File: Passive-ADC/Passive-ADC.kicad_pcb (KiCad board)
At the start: 2 copper layers, 72.6 x 24.1 mm, 11 parts, among them J1 FPGA Terminal, J2 ADC Terminal

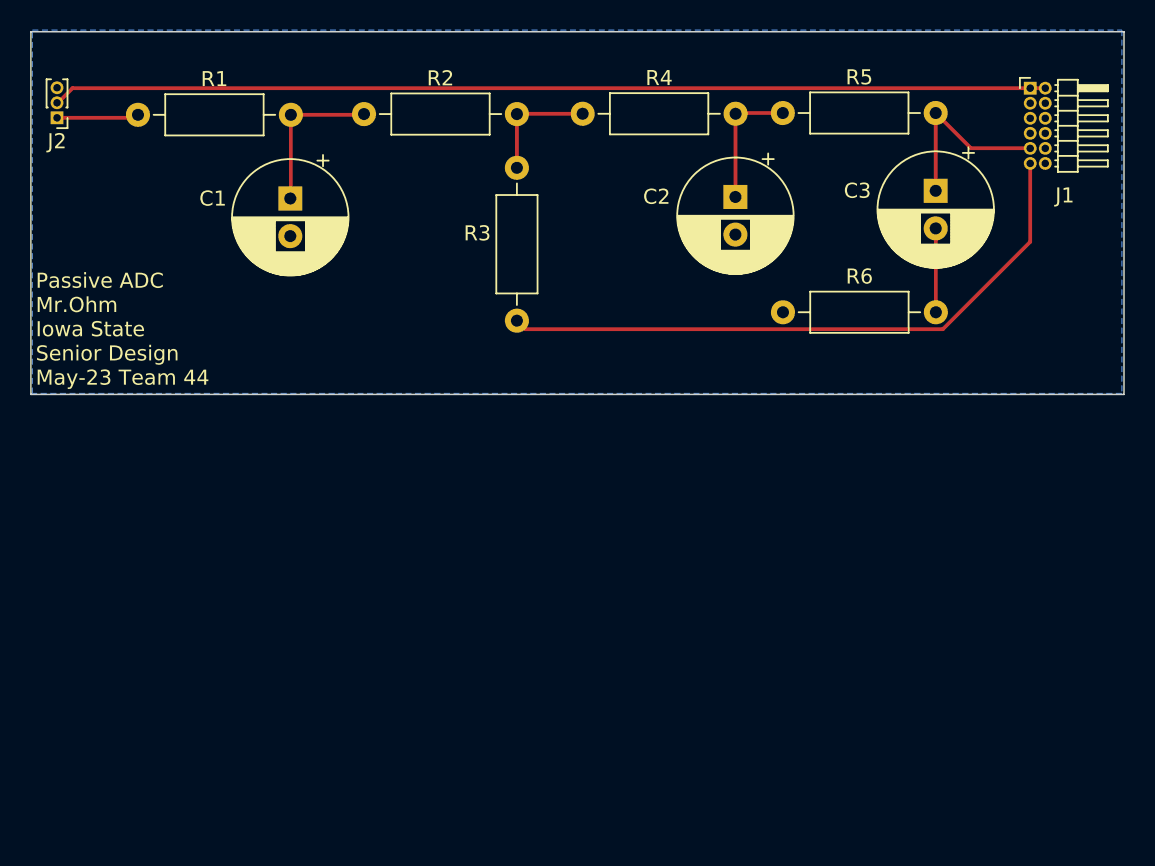
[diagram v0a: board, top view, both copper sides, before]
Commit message: Replaced passive adc with active adc
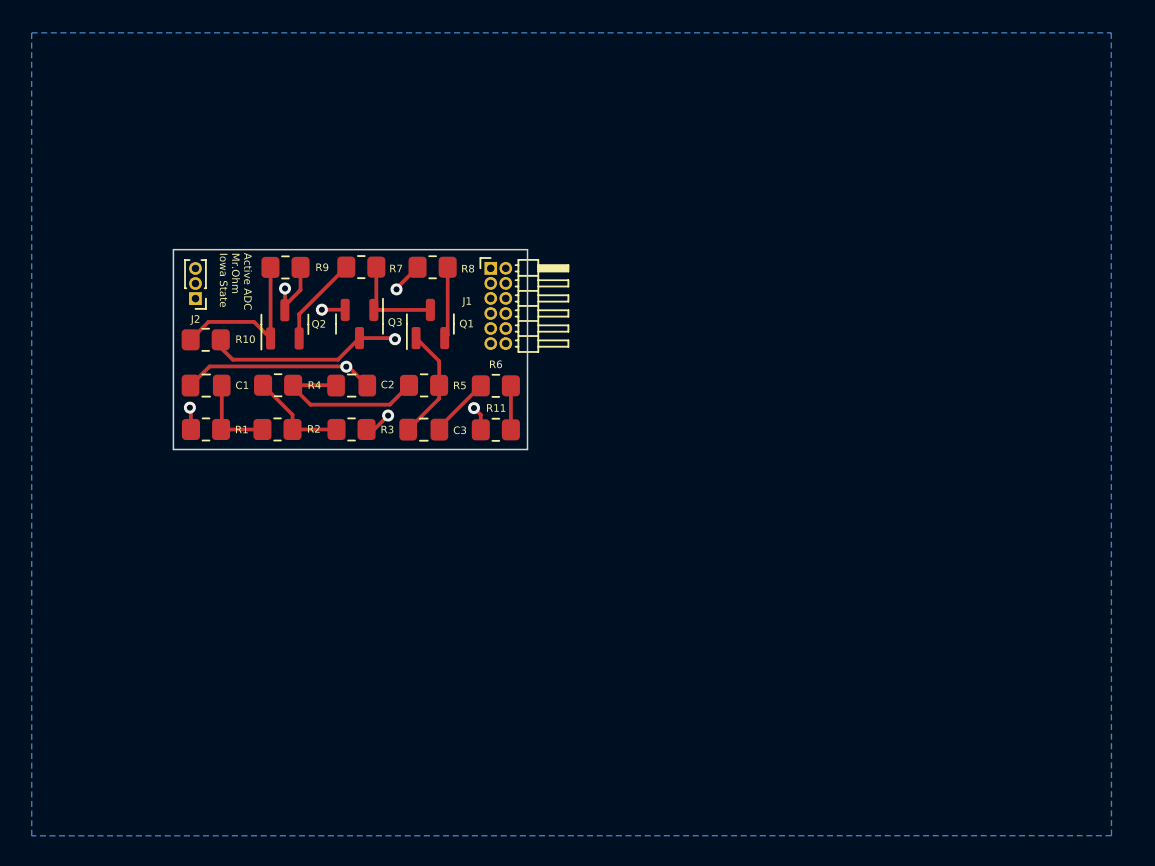
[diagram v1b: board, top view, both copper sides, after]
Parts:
- added Q1: BC847, Package_TO_SOT_SMD:SOT-23, F.Cu at (131.4, 85.2)
- added Q2: BC847, Package_TO_SOT_SMD:SOT-23, F.Cu at (121.7, 85.3)
- added Q3: BC847, Package_TO_SOT_SMD:SOT-23, F.Cu at (126.7, 85.2)
- added R10: 2.5k, Resistor_SMD:R_0805_2012Metric_Pad1.20x1.40mm_HandSolder, F.Cu at (116.5, 86.3)
- added R11: 680, Resistor_SMD:R_0805_2012Metric_Pad1.20x1.40mm_HandSolder, F.Cu at (135.7, 92.3)
- added R7: 2.1k, Resistor_SMD:R_0805_2012Metric_Pad1.20x1.40mm_HandSolder, F.Cu at (126.8, 81.5)
- added R8: 330, Resistor_SMD:R_0805_2012Metric_Pad1.20x1.40mm_HandSolder, F.Cu at (131.5, 81.5)
- added R9: 1.5k, Resistor_SMD:R_0805_2012Metric_Pad1.20x1.40mm_HandSolder, F.Cu at (121.8, 81.5)
- C1, C2, C3: footprint Capacitor_THT:CP_Radial_D7.5mm_P2.50mm -> Capacitor_SMD:C_0805_2012Metric_Pad1.18x1.45mm_HandSolder
- R1: footprint Resistor_THT:R_Axial_DIN0207_L6.3mm_D2.5mm_P10.16mm_Horizontal -> Resistor_SMD:R_0805_2012Metric_Pad1.20x1.40mm_HandSolder
- R2: value 36k -> 18k; footprint Resistor_THT:R_Axial_DIN0207_L6.3mm_D2.5mm_P10.16mm_Horizontal -> Resistor_SMD:R_0805_2012Metric_Pad1.20x1.40mm_HandSolder
- R3, R4: value 18k -> 15k; footprint Resistor_THT:R_Axial_DIN0207_L6.3mm_D2.5mm_P10.16mm_Horizontal -> Resistor_SMD:R_0805_2012Metric_Pad1.20x1.40mm_HandSolder
- R5: value 56k -> 8k; footprint Resistor_THT:R_Axial_DIN0207_L6.3mm_D2.5mm_P10.16mm_Horizontal -> Resistor_SMD:R_0805_2012Metric_Pad1.20x1.40mm_HandSolder
- R6: value 110 -> 470; footprint Resistor_THT:R_Axial_DIN0207_L6.3mm_D2.5mm_P10.16mm_Horizontal -> Resistor_SMD:R_0805_2012Metric_Pad1.20x1.40mm_HandSolder
- moved J1 37.8 mm to (135.4, 81.5)
- moved C3 37.5 mm to (130.9, 92.3), turned to 0 degrees
- moved R5 29.9 mm to (131.0, 89.3)
- moved C2 28.4 mm to (126.2, 89.3), turned to 0 degrees
- moved R4 27.1 mm to (121.3, 89.3)
- moved R2 21.7 mm to (121.2, 92.3)
- moved R1 21.4 mm to (116.5, 92.3)
- moved R6 19.7 mm to (135.7, 89.4), turned to 180 degrees
- moved J2 15.1 mm to (115.8, 83.6)
- moved C1 13.6 mm to (116.5, 89.3), turned to 180 degrees
- moved R3 13.2 mm to (126.2, 92.3), turned to 180 degrees
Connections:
- C3 pad 1: /FPGA-OUT -> /SIGMA-CHERRY
- R5 pad 2: /FPGA-OUT -> /SIGMA-CHERRY
- R6 pad 1: GND -> Net-(R6-Pad1)
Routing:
- net /3.3V: track 66.1 -> 4.72 mm, vias 0 -> 1
- net /FPGA-IN: track 42.0 -> 10.6 mm, vias 0 -> 1
- net GND: track 0.00 -> 18.0 mm, vias 0 -> 4
- net Net-(Q2-Pad1): track 0.00 -> 11.0 mm
- net /SIGMA-CHERRY: track 0.00 -> 7.57 mm
- net /FPGA-OUT: track 12.7 -> 19.7 mm, vias 0 -> 1
- net Net-(Q1-Pad3): track 0.00 -> 6.70 mm
- net Net-(Q2-Pad2): track 0.00 -> 6.04 mm
- net Net-(Q1-Pad2): track 0.00 -> 4.79 mm
- net Net-(C1-Pad1): track 10.5 -> 5.69 mm
- net /Sensor-IN: track 5.46 -> 8.88 mm, vias 0 -> 1
- net Net-(C2-Pad1): track 8.69 -> 11.7 mm
- net Net-(R6-Pad1): track 0.00 -> 2.92 mm
- net Net-(C3-Pad2): track 5.58 -> 4.05 mm
- net Net-(R2-Pad2): track 7.95 -> 6.67 mm
- added copper zone on In1.Cu, net /3.3V
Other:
- board size 72.6 x 24.1 mm -> 23.5 x 13.3 mm
- copper layers 2 -> 4
- board text added: "Active ADC Mr.Ohm Iowa State"
- board text removed: "Passive ADC Mr.Ohm Iowa State Senior Design May-23 Team 44"

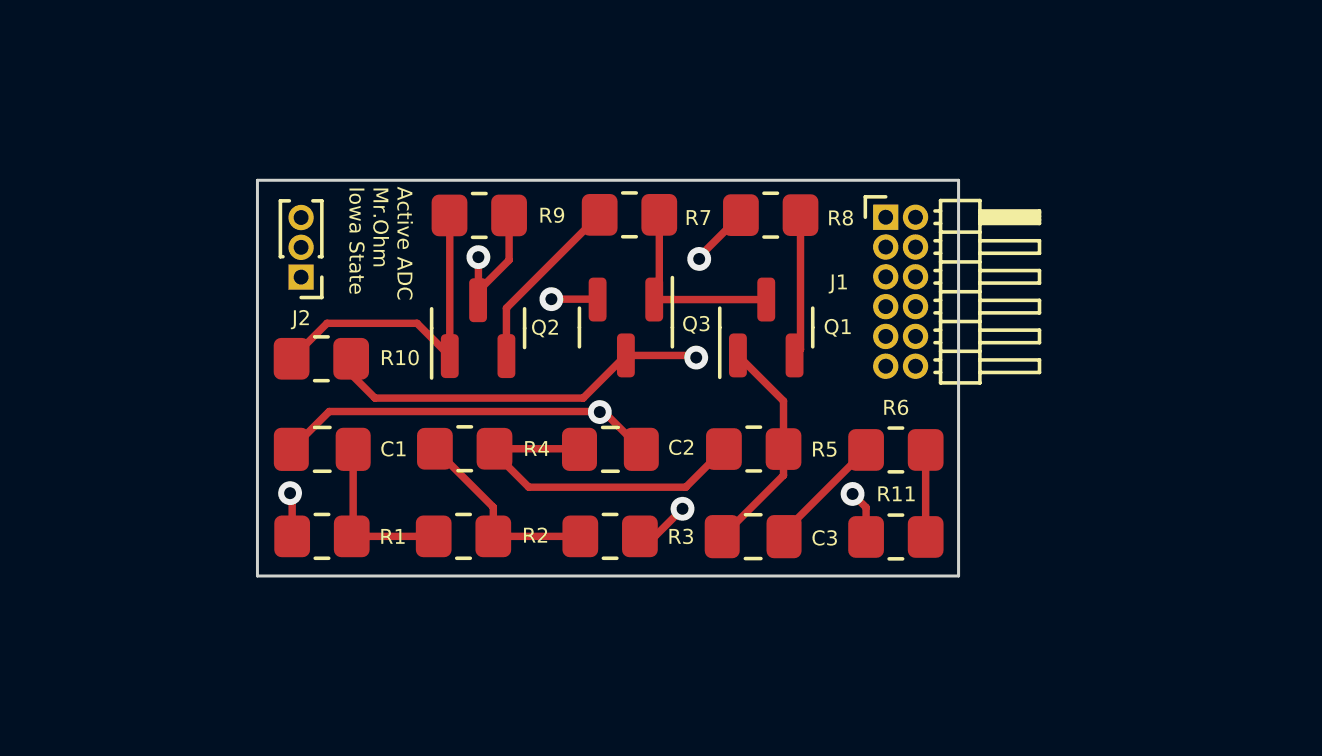
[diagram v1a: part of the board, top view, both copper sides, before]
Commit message: Update passive curcuit with new resistor values
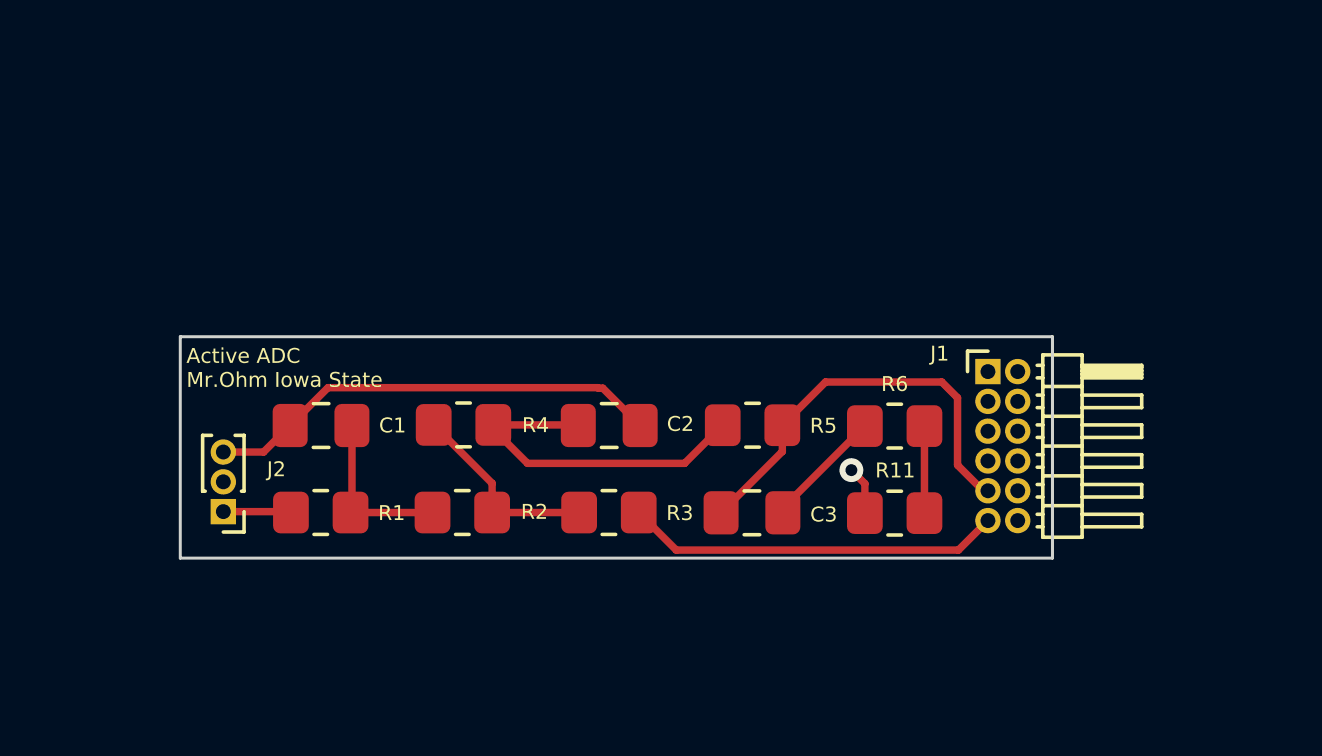
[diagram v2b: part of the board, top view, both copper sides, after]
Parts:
- removed Q1, Q2, Q3: BC847, Package_TO_SOT_SMD:SOT-23
- removed R10: 2.5k, Resistor_SMD:R_0805_2012Metric_Pad1.20x1.40mm_HandSolder
- removed R7: 2.1k, Resistor_SMD:R_0805_2012Metric_Pad1.20x1.40mm_HandSolder
- removed R8: 330, Resistor_SMD:R_0805_2012Metric_Pad1.20x1.40mm_HandSolder
- removed R9: 1.5k, Resistor_SMD:R_0805_2012Metric_Pad1.20x1.40mm_HandSolder
- moved J2 8.29 mm to (113.2, 91.4)
- moved J1 6.21 mm to (138.8, 86.7)
- moved R1 0.80 mm to (116.4, 91.5)
- moved R2 0.80 mm to (121.2, 91.5)
- moved R3 0.80 mm to (126.1, 91.5)
- moved R11 0.80 mm to (135.7, 91.5)
- moved R6 0.80 mm to (135.7, 88.6)
- moved C1 0.80 mm to (116.5, 88.5)
- moved C2 0.80 mm to (126.1, 88.5)
- moved C3 0.80 mm to (130.9, 91.5)
- moved R4 0.80 mm to (121.2, 88.5)
- moved R5 0.80 mm to (130.9, 88.5)
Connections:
- C3 pad 1: /SIGMA-CHERRY -> /FPGA-OUT
- R5 pad 2: /SIGMA-CHERRY -> /FPGA-OUT
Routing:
- net Net-(Q2-Pad1): track 11.0 -> 0.00 mm
- net /SIGMA-CHERRY: track 7.57 -> 0.00 mm
- net Net-(Q1-Pad3): track 6.70 -> 0.00 mm
- net /Sensor-IN: track 8.88 -> 2.28 mm, vias 1 -> 0
- net Net-(Q2-Pad2): track 6.04 -> 0.00 mm
- net /FPGA-OUT: track 19.7 -> 14.1 mm, vias 1 -> 0
- net Net-(Q1-Pad2): track 4.79 -> 0.00 mm
- net /3.3V: track 4.72 -> 0.00 mm, vias 1 -> 0
- net /FPGA-IN: track 10.6 -> 12.7 mm, vias 1 -> 0
- net GND: track 18.0 -> 17.0 mm, vias 4 -> 1
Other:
- board size 23.5 x 13.3 mm -> 29.3 x 7.4 mm

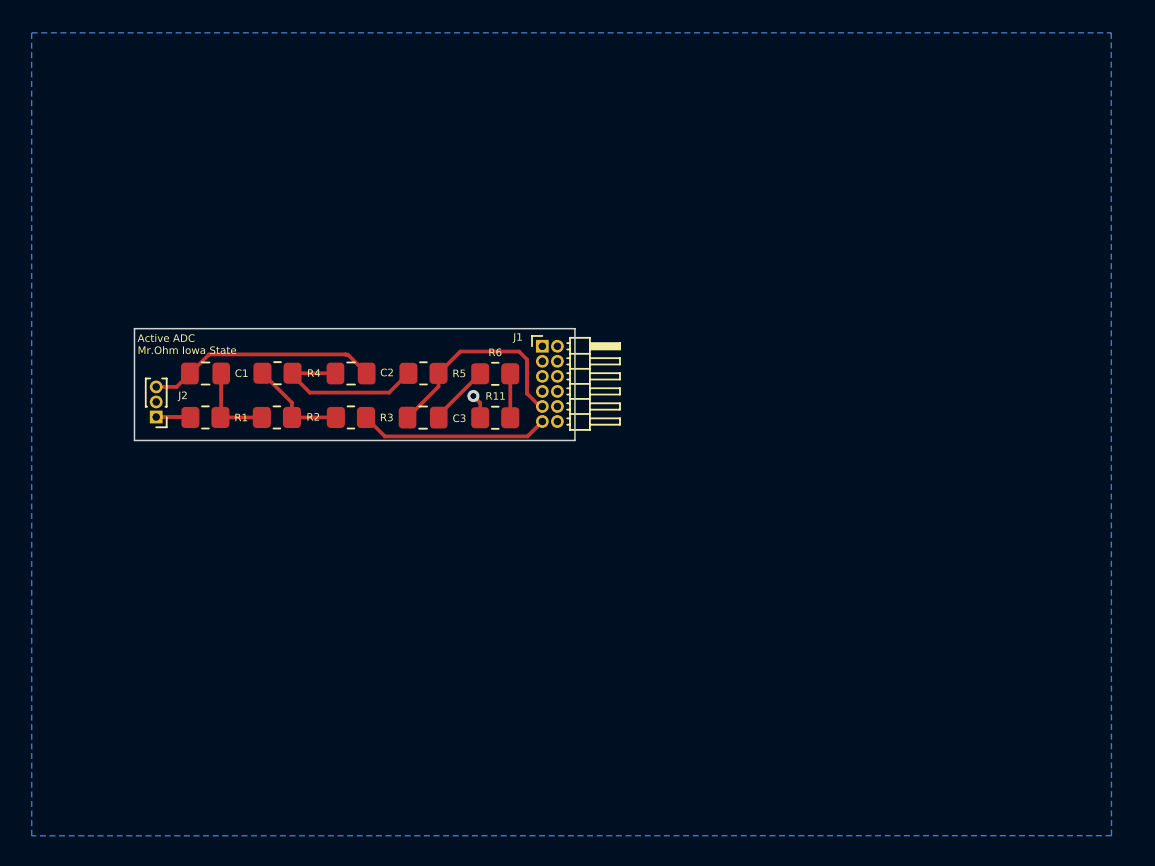
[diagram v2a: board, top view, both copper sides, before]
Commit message: Close to final pcb adjusted footprints and layout design incorperating voltage divider
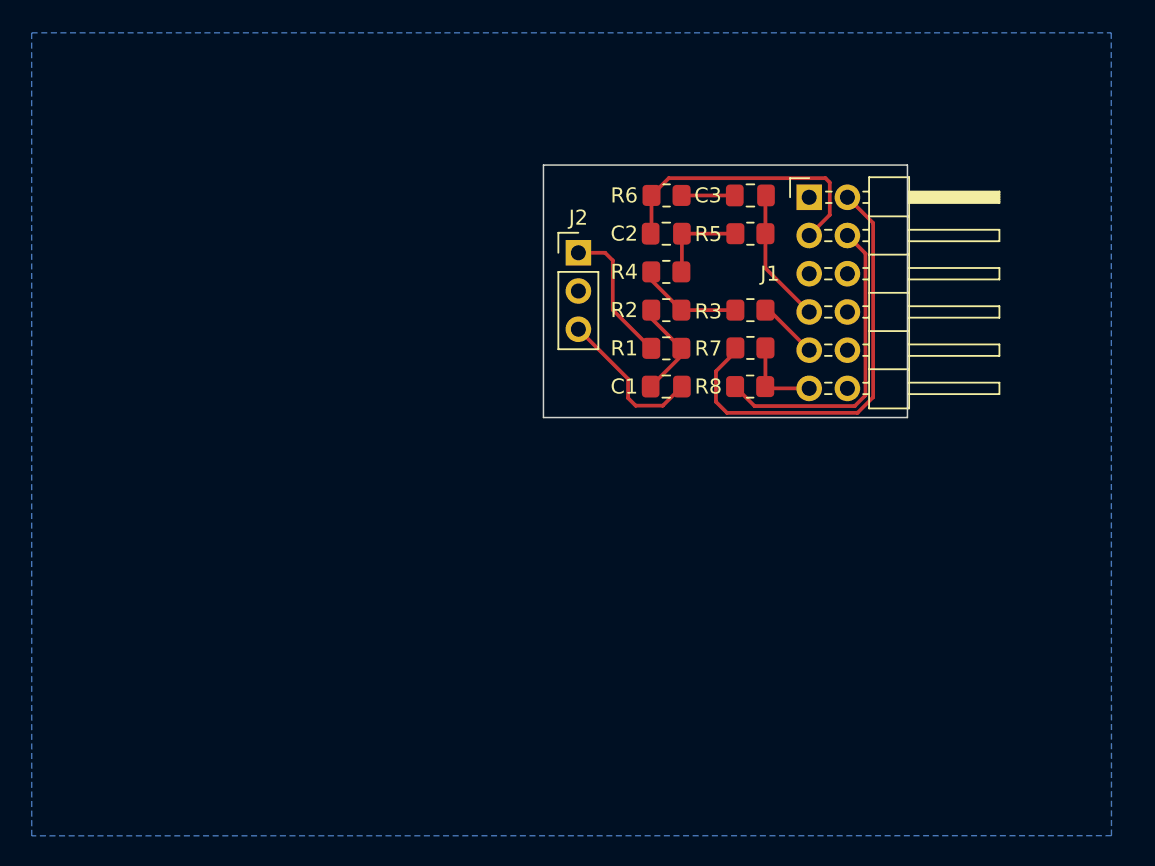
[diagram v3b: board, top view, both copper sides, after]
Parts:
- removed R11: 680, Resistor_SMD:R_0805_2012Metric_Pad1.20x1.40mm_HandSolder
- added R7: 6.8k, Resistor_SMD:R_0805_2012Metric_Pad1.20x1.40mm_HandSolder, F.Cu at (152.7, 86.8)
- added R8: 3.3k, Resistor_SMD:R_0805_2012Metric_Pad1.20x1.40mm_HandSolder, F.Cu at (152.6, 89.4)
- J1: footprint Connector_PinHeader_1.00mm:PinHeader_2x06_P1.00mm_Horizontal -> Connector_PinHeader_2.54mm:PinHeader_2x06_P2.54mm_Horizontal
- J2: footprint Connector_PinHeader_1.00mm:PinHeader_1x03_P1.00mm_Vertical -> Connector_PinHeader_2.54mm:PinHeader_1x03_P2.54mm_Vertical
- R6: value 470 -> 1.1k
- moved R1 31.0 mm to (147.1, 86.9)
- moved C1 30.6 mm to (147.1, 89.4), turned to 0 degrees
- moved J2 30.1 mm to (141.2, 80.5), turned to 0 degrees
- moved R3 27.5 mm to (152.7, 84.3)
- moved R2 26.8 mm to (147.1, 84.3)
- moved R4 26.7 mm to (147.1, 81.8)
- moved C3 26.3 mm to (152.7, 76.7), turned to 180 degrees
- moved R5 23.6 mm to (152.7, 79.2)
- moved C2 22.9 mm to (147.1, 79.2), turned to 180 degrees
- moved J1 20.3 mm to (156.6, 76.8)
- moved R6 16.4 mm to (147.1, 76.7), turned to 0 degrees
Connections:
- J1 pad 11: /FPGA-IN -> /FPGA-REF
- J1 pad 7: unconnected-(J1-Pad7) -> /FPGA-OUT
- J1 pad 9: /FPGA-OUT -> /FPGA-IN
- R6 pad 1: Net-(R11-Pad2) -> GND
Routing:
- net GND: track 17.0 -> 50.0 mm, vias 1 -> 0
- net /3.3V: track 0.00 -> 29.3 mm
- net /FPGA-IN: track 12.7 -> 4.01 mm
- net /Sensor-IN: track 2.28 -> 9.40 mm
- net Net-(C2-Pad1): track 11.7 -> 6.11 mm
- net /FPGA-REF: track 0.00 -> 5.55 mm
- net /FPGA-OUT: track 14.1 -> 9.04 mm
- net Net-(R11-Pad2): track 2.92 -> 0.00 mm
- net Net-(C1-Pad1): track 5.69 -> 6.75 mm
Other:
- board size 29.3 x 7.4 mm -> 24.2 x 16.8 mm
- board text removed: "Active ADC Mr.Ohm Iowa State"
